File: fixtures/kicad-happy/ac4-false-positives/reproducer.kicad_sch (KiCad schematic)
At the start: 23 parts, among them J1 OwnedConn2, Q1 OwnedPMOS, Q2 OwnedPMOS, U1 OwnedBuck, U10 OwnedLoad, U2 OwnedLDO, U3 OwnedRefBuffer, U4 OwnedADC, U5 OwnedLoad, U6 OwnedMCU, U7 LSM6DSO32, U8 OwnedLoad, U9 LSM6DSO32

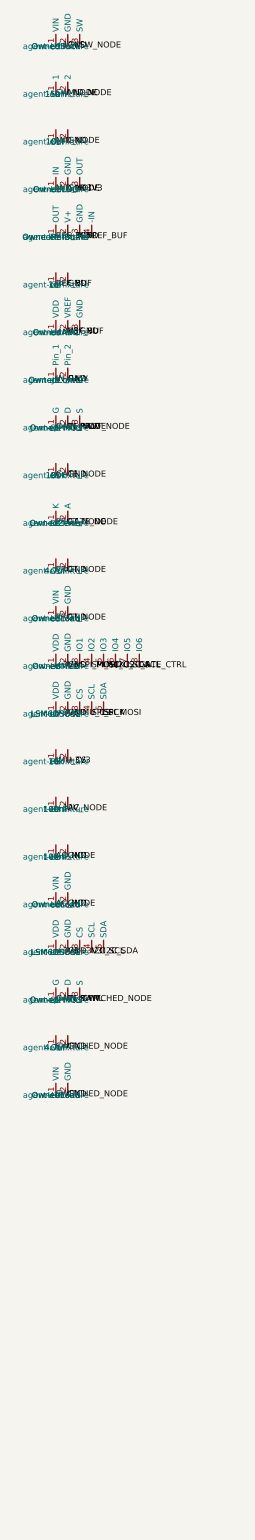
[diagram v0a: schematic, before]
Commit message: AGENTEE-219: target the conservative kicad-happy correction 33f2b48; add agent-469 controls
The reproducer test now targets kicad-happy 33f2b48 (branch
fix/pod-ac4-false-positives-c, installation 0220544c...), which supersedes
b8ab8b4. b8ab8b4 cleared both agent-469 adversarial controls and is recorded
as superseded. Pinned 2.3.1 stays a known limitation, never a pass.

- Reproducer: adds control (1), a P-MOSFET gate divider (100 ohm to the
  source, 1 Mohm to ground), and control (2), an I2C device whose CS has a
  passive 10k pull-up and an MCU GPIO. The SPI-wired IMU gains an owned SPI
  peer on its clock and data nets, the positive evidence the corrected rule
  needs.
- The test asserts the corrected errors equal the real violations plus both
  controls. Each cleared PP-001 limitation must be an info note with its
  exact assumptions, and the SPI note must cite its evidence. The PP-001
  unresolved conduction reasons are asserted.
- Severity gate: stale false_positive dispositions naming the limitation
  ids (reused on corrected PP-001 info notes with a new severity) attach to
  nothing and are reported in unused_disposition_ids, on both installs.
- A missing corrected commit in the AGENT_EE_KICAD_HAPPY object store fails
  under AGENT_EE_REQUIRE_TOOLCHAIN=1 with the commit, branch, store and the
  fix. It skips only outside strict mode, and a test covers both paths.
  Documented in docs/happy-severity-gate.md.

Co-Authored-By: Claude Opus 5.5 <noreply@anthropic.com>
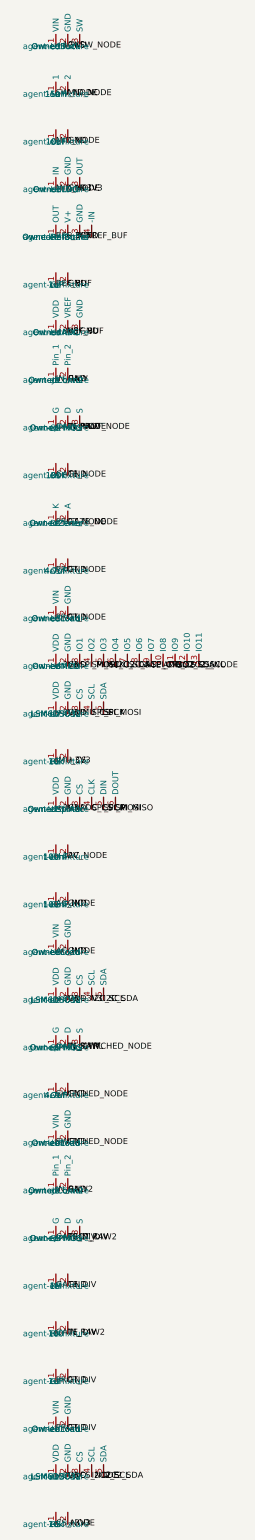
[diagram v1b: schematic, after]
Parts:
- added C7: 1uF, symbol Owned:OwnedC
- added J2: OwnedConn2, symbol Owned:OwnedConn2
- added Q3: OwnedPMOS, symbol Owned:Q_PMOS_Owned
- added R3: 1M, symbol Owned:OwnedR
- added R4: 100, symbol Owned:OwnedR
- added R5: 10k, symbol Owned:OwnedR
- added U11: OwnedLoad, symbol Owned:OwnedLoad
- added U12: LSM6DSO32, symbol Owned:OwnedIMU
- added U13: OwnedSpiAdc, symbol Owned:OwnedSpiAdc
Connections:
- net +3V3: now also R5.2, U12.1 (VDD), U13.1 (VDD)
- net GND: now also C7.2, J2.2 (Pin_2), R3.2, U11.2 (GND), U12.2 (GND), U13.2 (GND)
- net SPI_MOSI: now also U13.5 (DIN)
- net SPI_SCK: now also U13.4 (CLK)
- new net ADC_CS: U13.3 (CS), U6.10 (IO8)
- new net CS_NODE: R5.1, U12.3 (CS), U6.13 (IO11)
- new net GATE_DIV: Q3.1 (G), R3.1, R4.1
- new net I2C2_SCL: U12.4 (SCL), U6.12 (IO10)
- new net I2C2_SDA: U12.5 (SDA), U6.11 (IO9)
- new net IN_RAW2: J2.1 (Pin_1), Q3.3 (S), R4.2
- new net PROT_DIV: C7.1, Q3.2 (D), U11.1 (VIN)
- new net SPI_MISO: U13.6 (DOUT), U6.9 (IO7)
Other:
- moved on the sheet: C4, C5, C6, Q2, U10, U8, U9
